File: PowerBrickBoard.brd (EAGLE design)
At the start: 60.3 x 40 mm, 7 parts

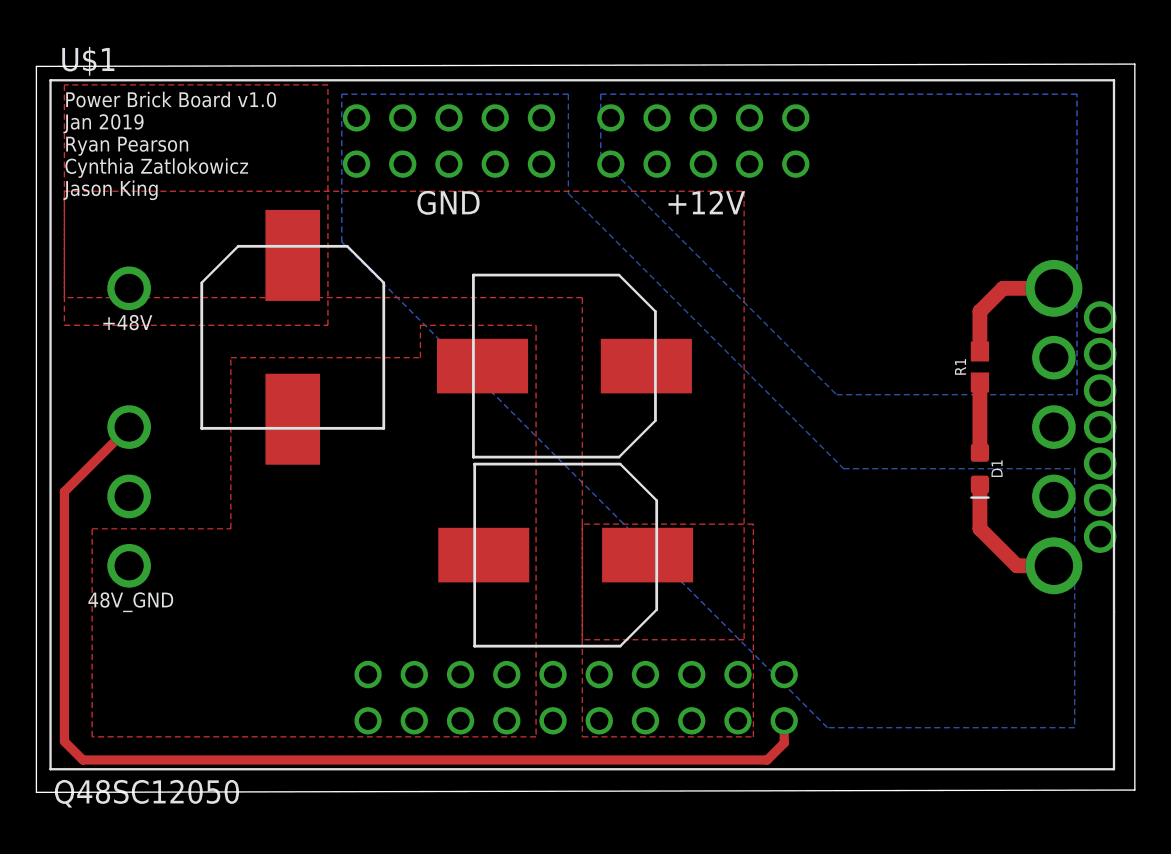
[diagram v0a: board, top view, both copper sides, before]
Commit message: Increased trace width of polygons.. we need it
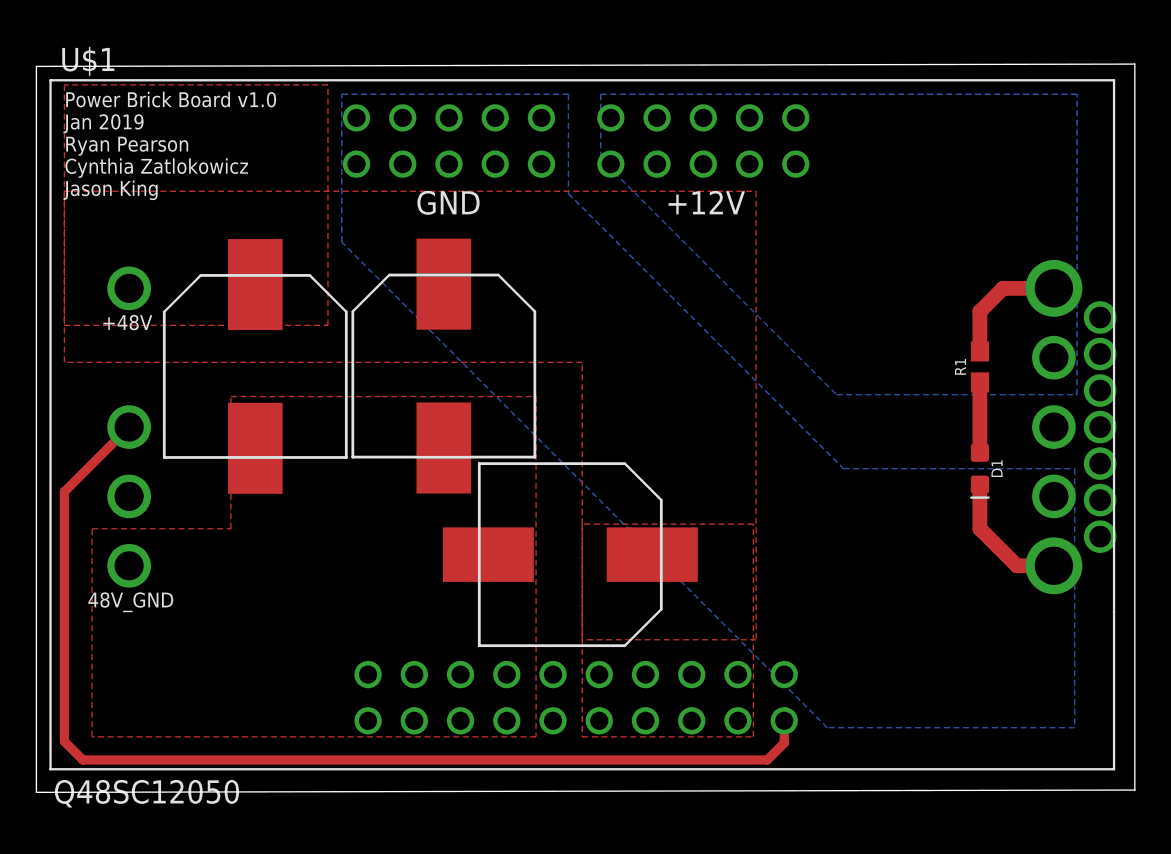
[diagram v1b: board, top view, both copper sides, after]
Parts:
- moved U$4 6.62 mm to (22.4, 23.4), turned to 0 degrees
- moved U$5 2.61 mm to (12.0, 23.4)
- moved U$3 0.26 mm to (29.3, 13.1)
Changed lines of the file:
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@@
 <?xml version="1.0" encoding="utf-8"?>
 <!DOCTYPE eagle SYSTEM "eagle.dtd">
-<eagle version="9.2.0">
+<eagle version="9.1.3">
 <drawing>
 <settings>
@@
 <element name="U$1" library="Q48SC12050" package="Q48SC12050" value="Q48SC12050" x="5.0927" y="27.686"/>
 <element name="U$2" library="PDB_TO_BRICKS" package="BRICK_TO_POWER_DIST_WHOLE" value="BRICK_TO_POWER_DIST_WHOLE" x="59.7027" y="0" rot="MR0"/>
-<element name="U$3" library="UCM1H331MNL1GS" package="UCM1H331MNL1GS" value="330 uF" x="29.0727" y="13.032" rot="R270"/>
-<element name="U$4" library="UCM1H331MNL1GS" package="UCM1H331MNL1GS" value="330 uF" x="29.0046375" y="23.41605625" rot="R270"/>
-<element name="U$5" library="UCM1H331MNL1GS" package="UCM1H331MNL1GS" value="330 uF" x="14.0807" y="24.996"/>
+<element name="U$3" library="UCM1H331MNL1GS" package="UCM1H331MNL1GS" value="330 uF" x="29.3267" y="13.0574" rot="R270"/>
+<element name="U$4" library="UCM1H331MNL1GS" package="UCM1H331MNL1GS" value="330 uF" x="22.38014375" y="23.4166375"/>
+<element name="U$5" library="UCM1H331MNL1GS" package="UCM1H331MNL1GS" value="330 uF" x="12.0233" y="23.3958"/>
 <element name="D1" library="SparkFun-LED" library_urn="urn:adsk.eagle:library:529" package="LED-0603" package3d_urn="urn:adsk.eagle:package:39354/1" value="" x="51.8287" y="17.78" rot="R270">
 <attribute name="NAME" x="52.4637" y="17.78" size="0.6096" layer="25" font="vector" ratio="20" rot="R270" align="bottom-center"/>
@@
 <contactref element="U$4" pad="P$2"/>
 <contactref element="U$5" pad="P$2"/>
-<polygon width="0.8128" layer="1" isolate="0.8128">
+<polygon width="0.8128" layer="1" isolate="0.8128" thermals="no">
 <vertex x="1.5367" y="33.02"/>
-<vertex x="38.8747" y="33.02"/>
-<vertex x="38.8747" y="8.382"/>
+<vertex x="39.5351" y="33.02"/>
+<vertex x="39.5351" y="8.382"/>
 <vertex x="29.9847" y="8.382"/>
-<vertex x="29.9847" y="27.178"/>
-<vertex x="1.5367" y="27.178"/>
+<vertex x="29.9847" y="23.622"/>
+<vertex x="1.5367" y="23.622"/>
 </polygon>
 <polygon width="0.8128" layer="1" isolate="0.8128" thermals="no">
@@
 <vertex x="3.0607" y="14.478"/>
 <vertex x="10.6807" y="14.478"/>
-<vertex x="10.6807" y="23.876"/>
-<vertex x="21.0947" y="23.876"/>
-<vertex x="21.0947" y="25.654"/>
-<vertex x="27.4447" y="25.654"/>
+<vertex x="10.6807" y="21.7424"/>
+<vertex x="18.9611" y="21.7424"/>
+<vertex x="27.4447" y="21.7424"/>
 <vertex x="27.4447" y="3.048"/>
 <vertex x="3.0607" y="3.048"/>

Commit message: rerouted the board
had to update the part so i had to move things around and redo the routing/polygons
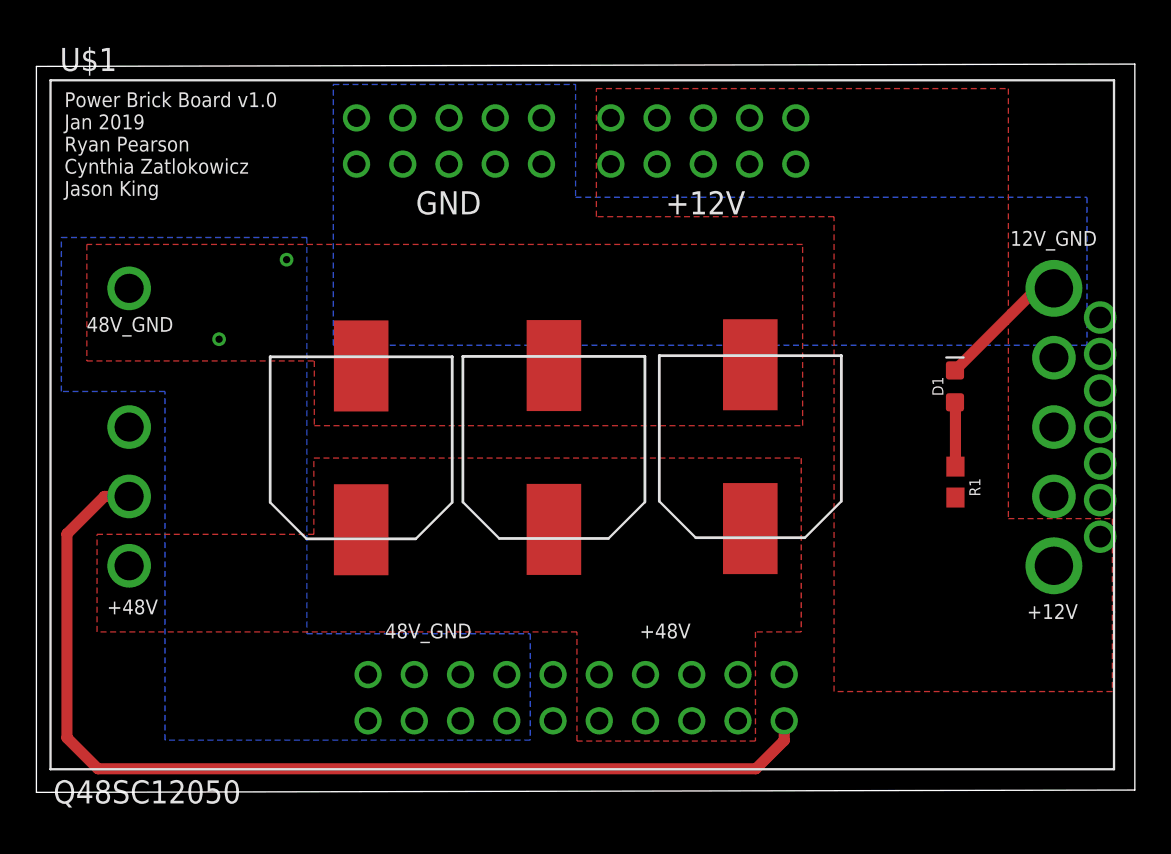
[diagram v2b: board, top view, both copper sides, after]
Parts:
- moved U$3 11.5 mm to (39.2, 19.0), turned to 180 degrees
- moved U$4 7.52 mm to (28.4, 18.9), turned to 180 degrees
- moved U$5 7.34 mm to (17.8, 18.9), turned to 180 degrees
- moved R1 6.47 mm to (50.5, 17.0), turned to 270 degrees
- moved D1 4.72 mm to (50.5, 22.3), turned to 90 degrees
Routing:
- net +12V: track 6.79 -> 0.00 mm
- net ON/OFF: track 60.3 -> 57.3 mm
- added copper zone on layer 1, net +12V
- added copper zone on layer 16, net 48V_GND
- removed copper zone on layer 16, net +12V
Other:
- board text added: "12V_GND"

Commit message: Updated name, moved some things
updated name to v1.1 and moved resistor and LED so the polygon for 12V was larger
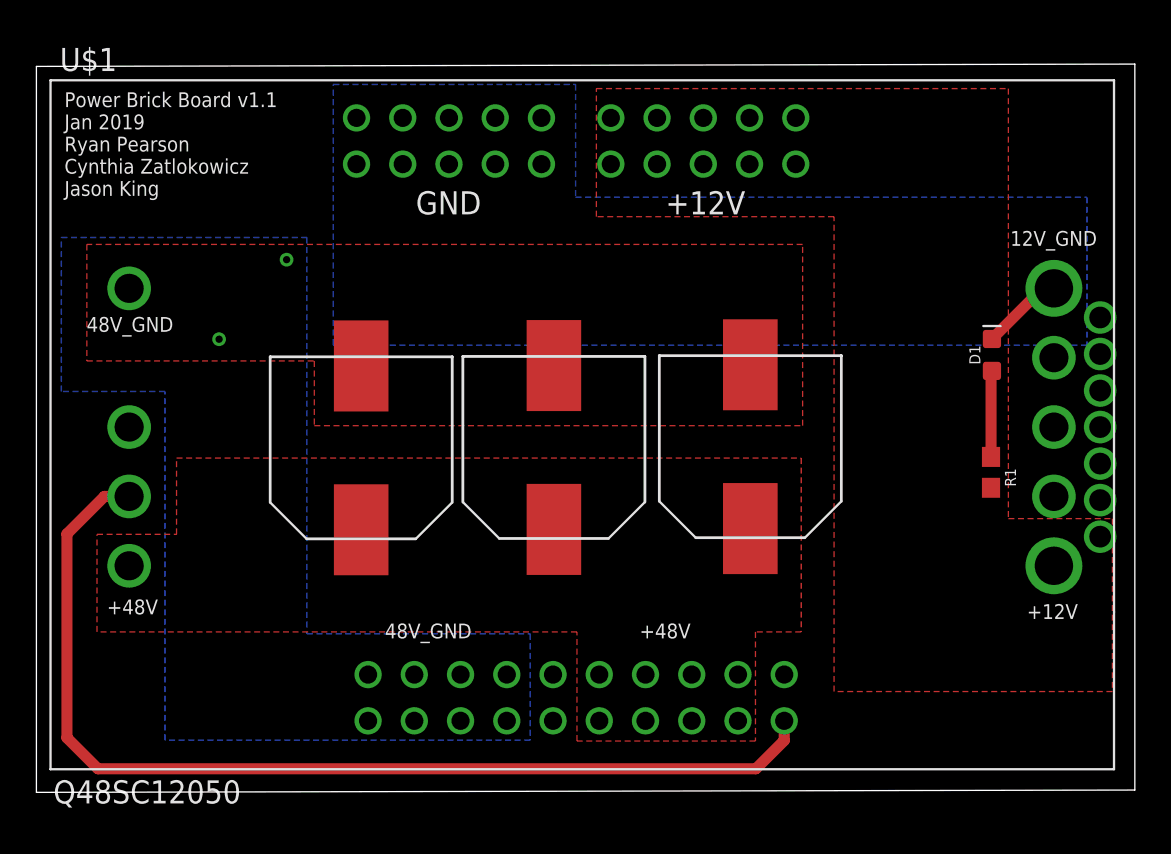
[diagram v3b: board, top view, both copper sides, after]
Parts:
- moved D1 2.67 mm to (52.5, 24.0)
- moved R1 2.03 mm to (52.4, 17.6)
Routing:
- net GND: track 7.30 -> 4.56 mm
- net N$1: track 3.54 -> 4.75 mm
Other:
- board text added: "Power Brick Board v1.1 Jan 2019 Ryan Pearson Cynthia Zatlokowicz Jason King"
- board text removed: "Power Brick Board v1.0 Jan 2019 Ryan Pearson Cynthia Zatlokowicz Jason King"
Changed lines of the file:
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@@
 <wire x1="60.3377" y1="40.005" x2="-0.0013" y2="39.878" width="0" layer="20"/>
 <wire x1="-0.0013" y1="39.878" x2="-0.0013" y2="0" width="0" layer="20"/>
-<text x="1.5367" y="32.766" size="0.8128" layer="21">Power Brick Board v1.0
+<text x="1.5367" y="32.766" size="0.8128" layer="21">Power Brick Board v1.1
 Jan 2019
 Ryan Pearson
@@
 <element name="U$4" library="UCM1H331MNL1GS" package="UCM1H331MNL1GS" value="330 uF" x="28.42534375" y="18.9462375" rot="R180"/>
 <element name="U$5" library="UCM1H331MNL1GS" package="UCM1H331MNL1GS" value="330 uF" x="17.8399" y="18.9254" rot="R180"/>
-<element name="D1" library="SparkFun-LED" library_urn="urn:adsk.eagle:library:529" package="LED-0603" package3d_urn="urn:adsk.eagle:package:39354/1" value="" x="50.4571" y="22.3012" rot="R90">
-<attribute name="NAME" x="49.8221" y="22.3012" size="0.6096" layer="25" font="vector" ratio="20" rot="R90" align="bottom-center"/>
-<attribute name="VALUE" x="51.0921" y="22.3012" size="0.6096" layer="27" font="vector" ratio="20" rot="R90" align="top-center"/>
+<element name="D1" library="SparkFun-LED" library_urn="urn:adsk.eagle:library:529" package="LED-0603" package3d_urn="urn:adsk.eagle:package:39354/1" value="" x="52.4891" y="24.0284" rot="R90">
+<attribute name="NAME" x="51.8541" y="24.0284" size="0.6096" layer="25" font="vector" ratio="20" rot="R90" align="bottom-center"/>
+<attribute name="VALUE" x="53.1241" y="24.0284" size="0.6096" layer="27" font="vector" ratio="20" rot="R90" align="top-center"/>
 </element>
-<element name="R1" library="SparkFun-Resistors" library_urn="urn:adsk.eagle:library:532" package="0603" package3d_urn="urn:adsk.eagle:package:39650/1" value=" 470" x="50.4825" y="17.0434" rot="R270">
-<attribute name="NAME" x="51.2445" y="16.764" size="0.6096" layer="25" font="vector" ratio="20" rot="R270" align="bottom-center"/>
-<attribute name="PROD_ID" value=" " x="50.4825" y="17.0434" size="1.778" layer="27" rot="R270" display="off"/>
-<attribute name="VALUE" x="49.7205" y="17.0434" size="0.6096" layer="27" font="vector" ratio="20" rot="R270" align="top-center"/>
+<element name="R1" library="SparkFun-Resistors" library_urn="urn:adsk.eagle:library:532" package="0603" package3d_urn="urn:adsk.eagle:package:39650/1" value=" 470" x="52.4383" y="17.5768" rot="R270">
+<attribute name="NAME" x="53.2003" y="17.2974" size="0.6096" layer="25" font="vector" ratio="20" rot="R270" align="bottom-center"/>
+<attribute name="PROD_ID" value=" " x="52.4383" y="17.5768" size="1.778" layer="27" rot="R270" display="off"/>
+<attribute name="VALUE" x="51.6763" y="17.5768" size="0.6096" layer="27" font="vector" ratio="20" rot="R270" align="top-center"/>
 </element>
 </elements>
@@
 <polygon width="0.508" layer="1" isolate="0.6096" thermals="no">
 <vertex x="3.3274" y="14.1732"/>
-<vertex x="15.24" y="14.1732"/>
-<vertex x="15.24" y="18.3642"/>
+<vertex x="7.6962" y="14.1732"/>
+<vertex x="7.6962" y="18.3642"/>
 <vertex x="42.0116" y="18.3642"/>
 <vertex x="42.0116" y="8.8138"/>
@@
 <vertex x="16.3068" y="24.5618"/>
 </polygon>
-<wire x1="55.8927" y1="27.686" x2="54.9649" y2="27.686" width="0.6096" layer="1"/>
-<wire x1="54.9649" y1="27.686" x2="50.4571" y2="23.1782" width="0.6096" layer="1"/>
+<wire x1="55.8927" y1="27.686" x2="55.2697" y2="27.686" width="0.6096" layer="1"/>
+<wire x1="55.2697" y1="27.686" x2="52.4891" y2="24.9054" width="0.6096" layer="1"/>
 </signal>
 <signal name="48V_GND">
@@
 <contactref element="D1" pad="A"/>
 <contactref element="R1" pad="1"/>
-<wire x1="50.4571" y1="21.4242" x2="50.4825" y2="21.3988" width="0.6096" layer="1"/>
-<wire x1="50.4825" y1="21.3988" x2="50.4825" y2="17.8934" width="0.6096" layer="1"/>
+<wire x1="52.4891" y1="23.1514" x2="52.4383" y2="23.1006" width="0.6096" layer="1"/>
+<wire x1="52.4383" y1="23.1006" x2="52.4383" y2="18.4268" width="0.6096" layer="1"/>
 </signal>
 </signals>
